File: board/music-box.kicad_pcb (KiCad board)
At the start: 2 copper layers, 100 x 50 mm, 22 parts, among them J1 SPEAKER, J2 MEM2061-01-188-00-A, J3 PWR, J4 BTN_PWR, J5 RFID, U1 MAX98357AETE+T, U2 SC0918

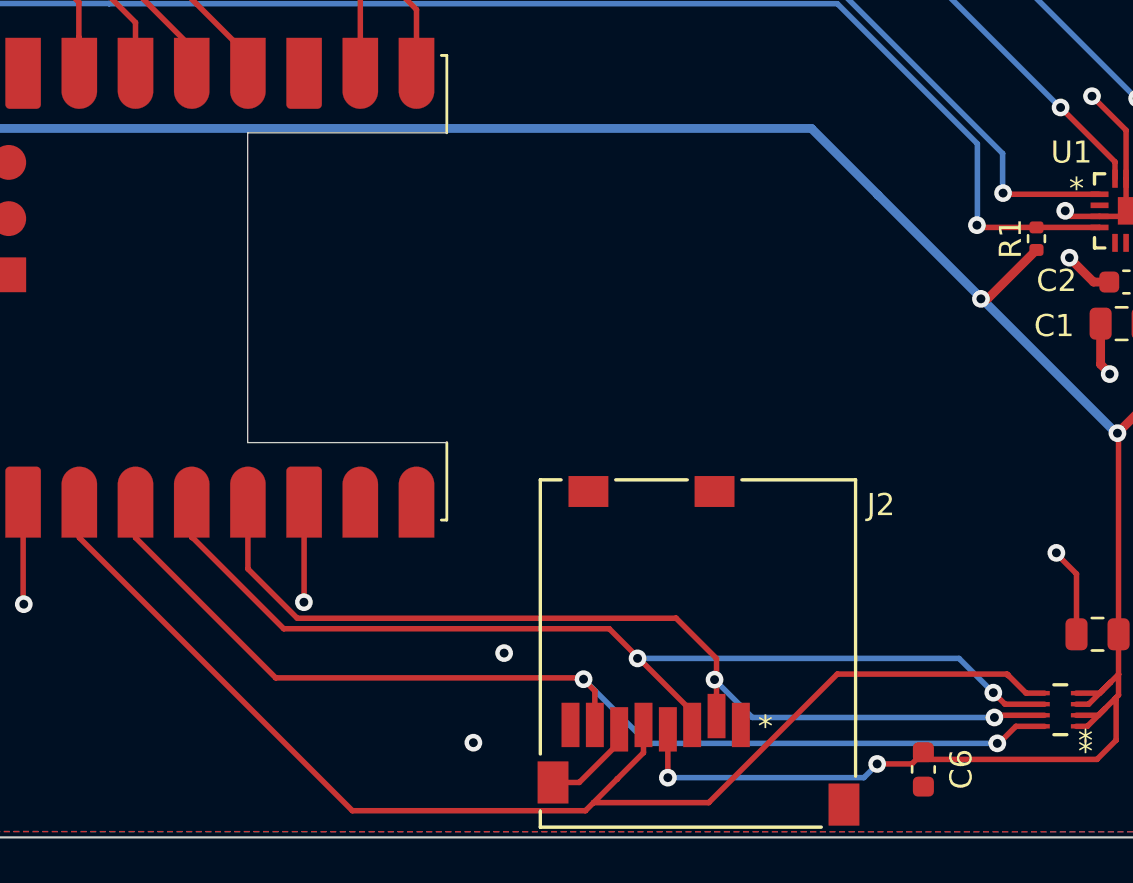
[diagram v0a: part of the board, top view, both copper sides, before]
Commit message: fixed issue with board (rx / tx swap for the sd card)
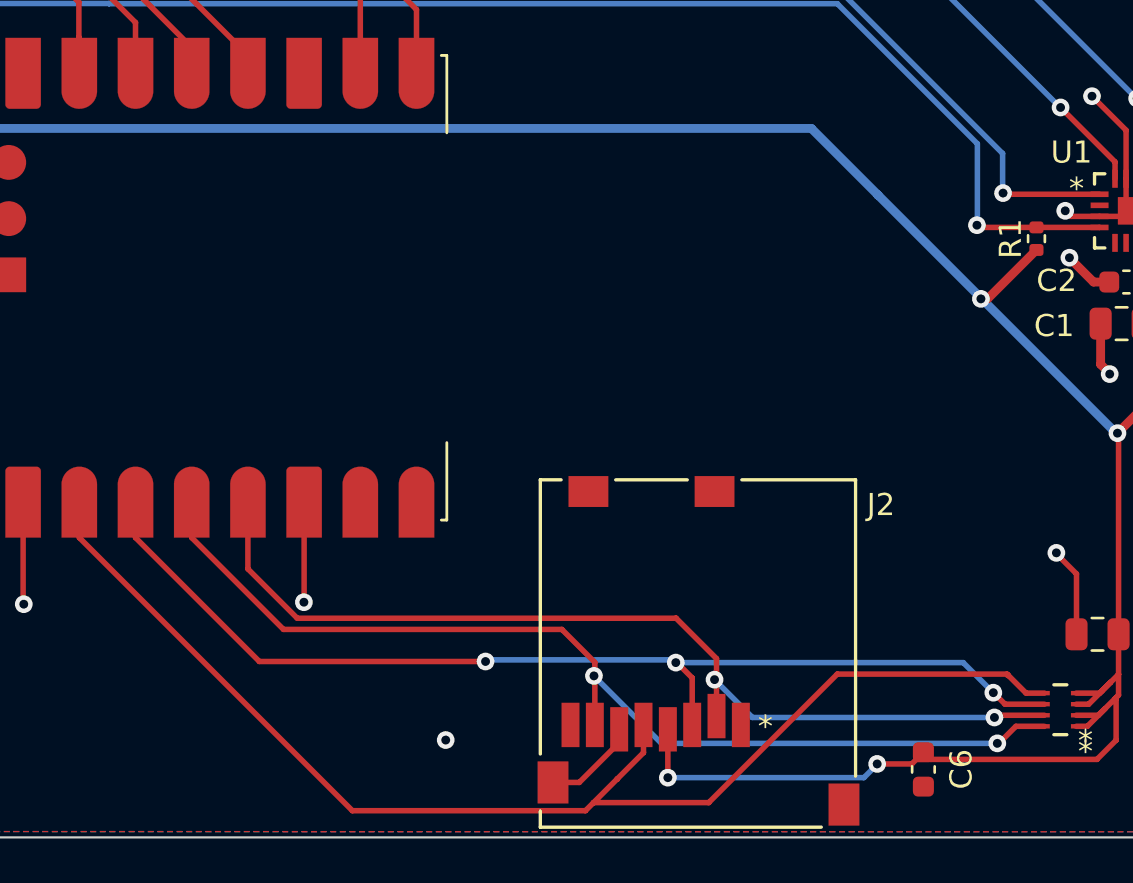
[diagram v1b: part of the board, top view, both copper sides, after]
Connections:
- J2 pad P3: /SD_RX -> /SD_MOSI
- J2 pad P7: /SD_TX -> /SD_MISO
- R2 pad 6: /SD_RX -> /SD_MOSI
- R2 pad 8: /SD_TX -> /SD_MISO
- U2 pad 15: /SD_TX -> /SD_MOSI
- U2 pad 16: /SD_RX -> /SD_MISO
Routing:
- net /SD_MOSI: track 0.00 -> 49.3 mm, vias 0 -> 3
- net /SD_TX: track 49.2 -> 0.00 mm, vias 2 -> 0
- net /SD_RX: track 49.0 -> 0.00 mm, vias 2 -> 0
- net /SD_MISO: track 0.00 -> 48.6 mm, vias 0 -> 2
- net GND: vias 13 -> 12
